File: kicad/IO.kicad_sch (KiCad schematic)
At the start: 40 parts, among them J3 Conn_02x10_Odd_Even, J4 Conn_02x10_Odd_Even, J5 Conn_02x10_Odd_Even, U12 ULN2803A

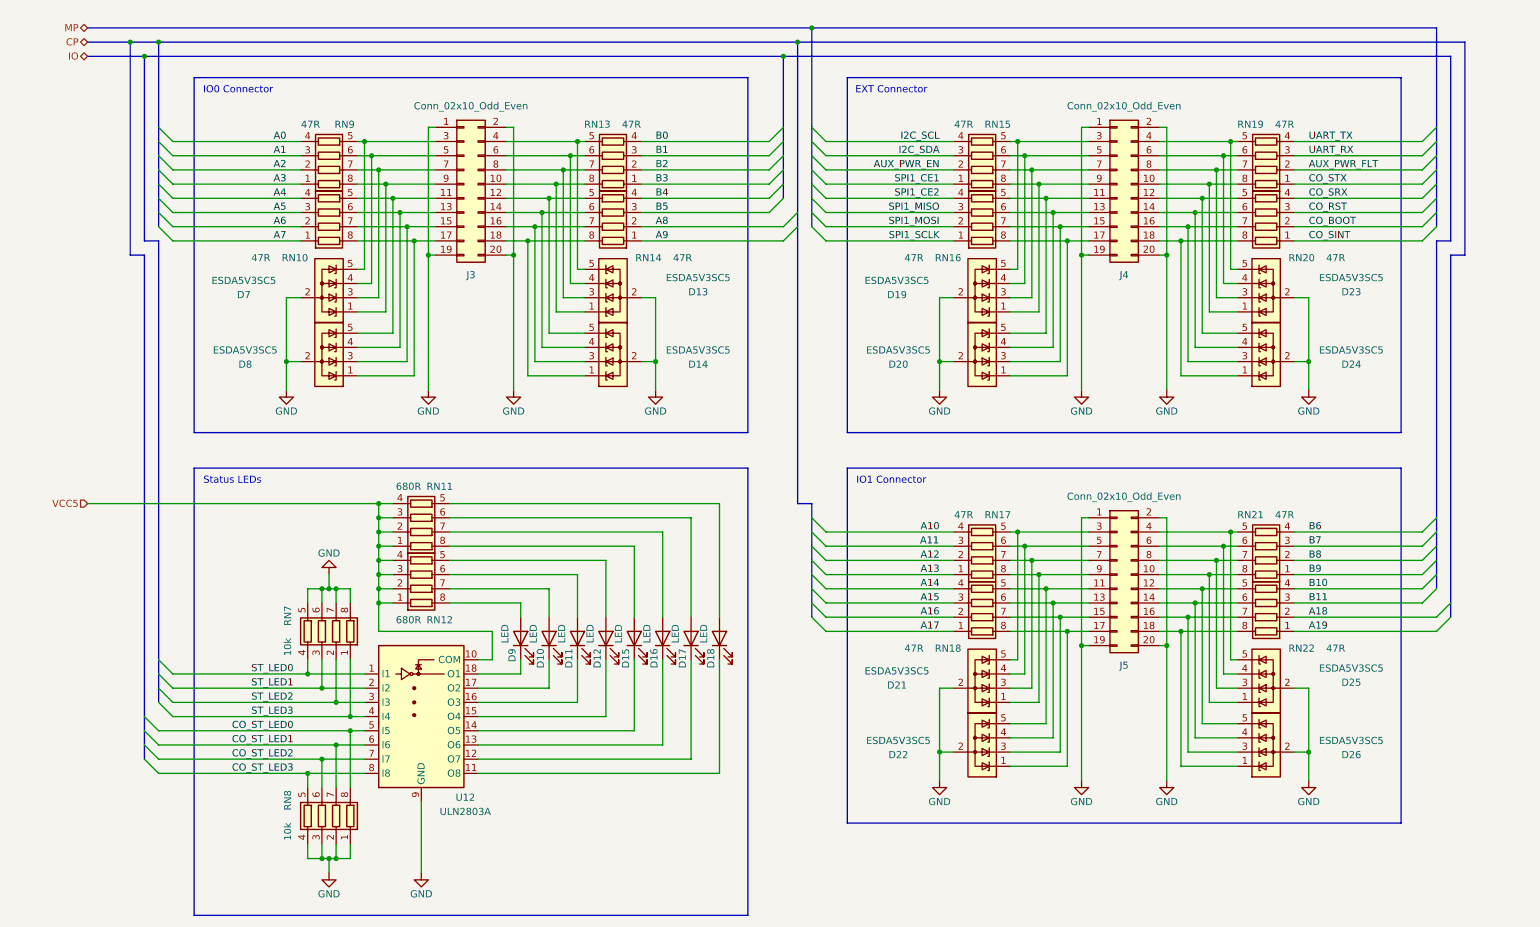
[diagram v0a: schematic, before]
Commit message: Add main bus to root schematic, use bus labels for exporting IO and CPIO busses
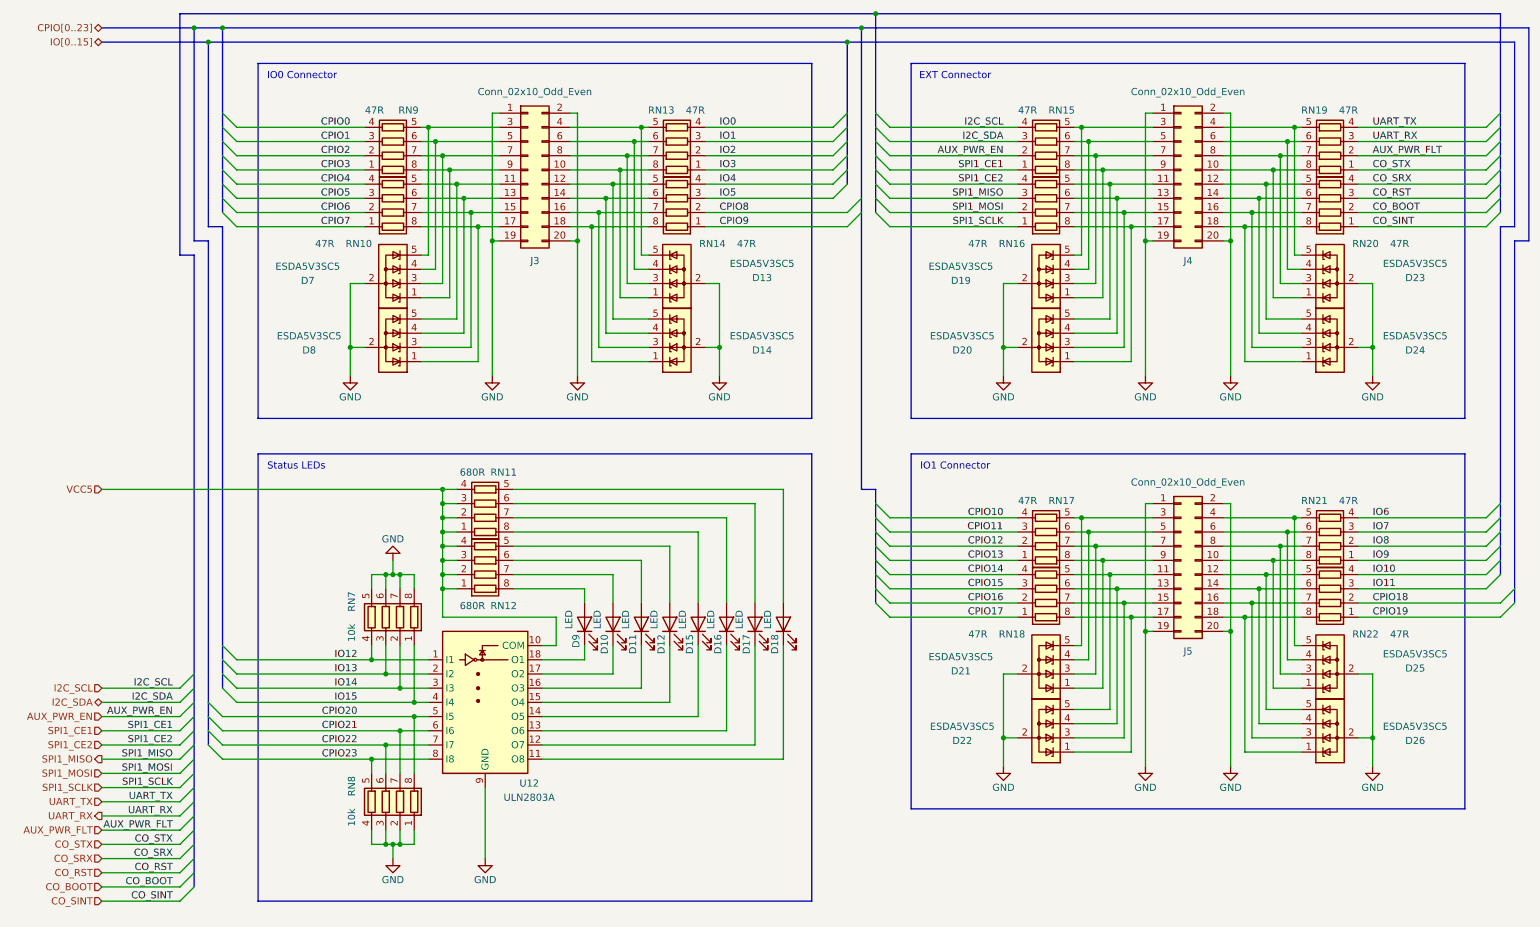
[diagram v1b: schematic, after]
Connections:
- net A0 renamed CPIO0
- net A1 renamed CPIO1
- net A10 renamed CPIO10
- net A11 renamed CPIO11
- net A12 renamed CPIO12
- net A13 renamed CPIO13
- net A14 renamed CPIO14
- net A15 renamed CPIO15
- net A16 renamed CPIO16
- net A17 renamed CPIO17
- net A18 renamed CPIO18
- net A19 renamed CPIO19
- net A2 renamed CPIO2
- net A3 renamed CPIO3
- net A4 renamed CPIO4
- net A5 renamed CPIO5
- net A6 renamed CPIO6
- net A7 renamed CPIO7
- net A8 renamed CPIO8
- net A9 renamed CPIO9
- net B0 renamed IO0
- net B1 renamed IO1
- net B10 renamed IO10
- net B11 renamed IO11
- net B2 renamed IO2
- net B3 renamed IO3
- net B4 renamed IO4
- net B5 renamed IO5
- net B6 renamed IO6
- net B7 renamed IO7
- net B8 renamed IO8
- net B9 renamed IO9
- net CO_ST_LED0 renamed CPIO20
- net CO_ST_LED1 renamed CPIO21
- net CO_ST_LED2 renamed CPIO22
- net CO_ST_LED3 renamed CPIO23
- net ST_LED0 renamed IO12
- net ST_LED1 renamed IO13
- net ST_LED2 renamed IO14
- net ST_LED3 renamed IO15
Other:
- moved on the sheet: D10, D11, D12, D13, D14, D15, D16, D17, D18, D19, D20, D21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

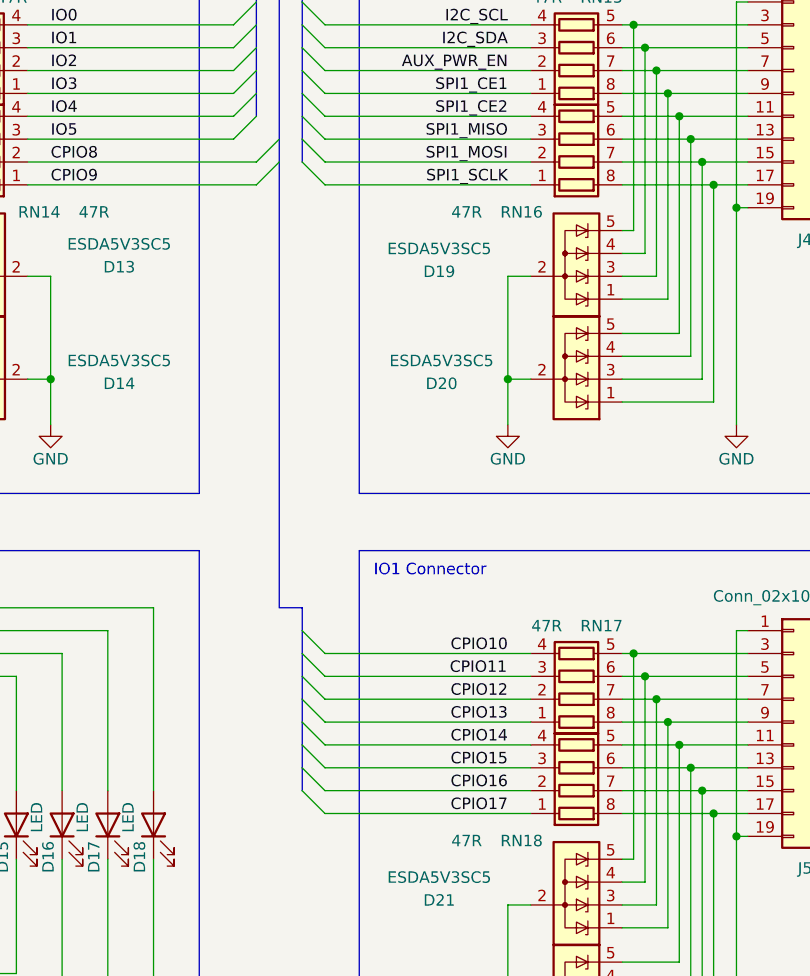
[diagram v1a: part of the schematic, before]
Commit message: Add EtherKraken V1 Rev. C schematics as PDF to docs
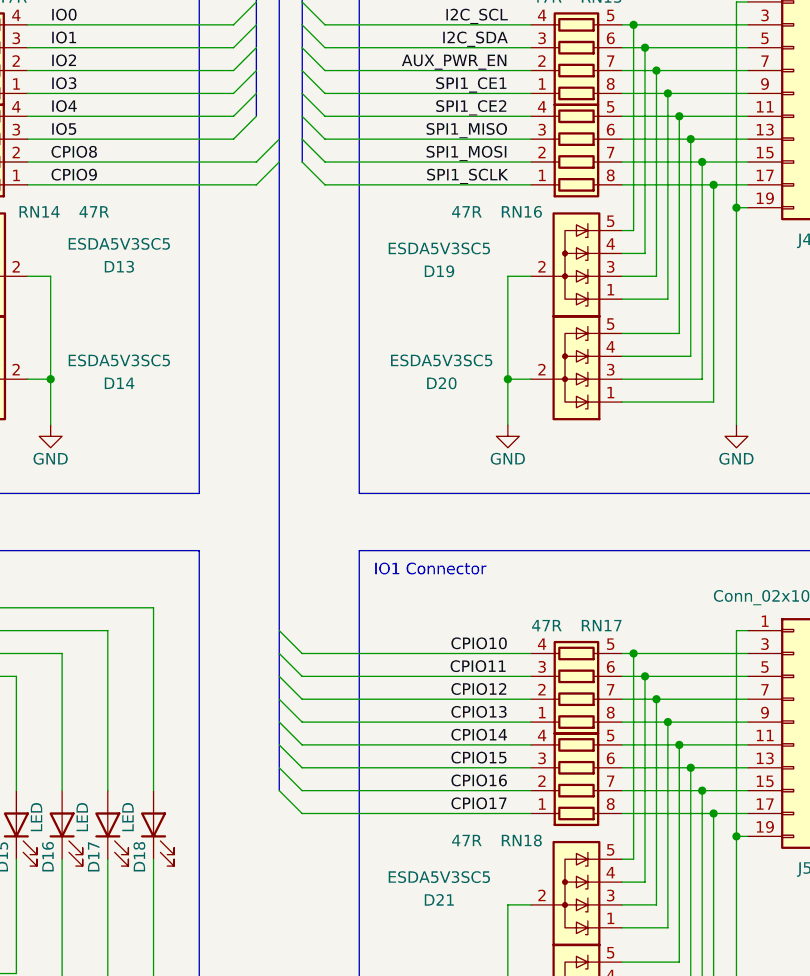
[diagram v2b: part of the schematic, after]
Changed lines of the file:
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@@
 	)
 	(bus_entry
-		(at 166.37 123.19)
+		(at 163.83 123.19)
 		(size 2.54 2.54)
 		(stroke
@@
 	)
 	(bus_entry
-		(at 166.37 105.41)
+		(at 163.83 105.41)
 		(size 2.54 2.54)
 		(stroke
@@
 	)
 	(bus_entry
-		(at 166.37 113.03)
+		(at 163.83 113.03)
 		(size 2.54 2.54)
 		(stroke
@@
 	)
 	(bus_entry
-		(at 166.37 120.65)
+		(at 163.83 120.65)
 		(size 2.54 2.54)
 		(stroke
@@
 	)
 	(bus_entry
-		(at 166.37 118.11)
+		(at 163.83 118.11)
 		(size 2.54 2.54)
 		(stroke
@@
 	)
 	(bus_entry
-		(at 166.37 110.49)
+		(at 163.83 110.49)
 		(size 2.54 2.54)
 		(stroke
@@
 	)
 	(bus_entry
-		(at 166.37 115.57)
+		(at 163.83 115.57)
 		(size 2.54 2.54)
 		(stroke
@@
 	)
 	(bus_entry
-		(at 166.37 107.95)
+		(at 163.83 107.95)
 		(size 2.54 2.54)
 		(stroke
@@
 	(wire
 		(pts
-			(xy 168.91 110.49) (xy 191.77 110.49)
+			(xy 166.37 110.49) (xy 191.77 110.49)
 		)
 		(stroke
@@
 	(wire
 		(pts
-			(xy 168.91 123.19) (xy 191.77 123.19)
+			(xy 166.37 123.19) (xy 191.77 123.19)
 		)
 		(stroke
@@
 		)
 	)
-	(bus
-		(pts
-			(xy 163.83 53.34) (xy 163.83 102.87)
-		)
-		(stroke
-			(width 0)
-			(type default)
-		)
-	)
 	(wire
 		(pts
@@
 	(wire
 		(pts
-			(xy 168.91 107.95) (xy 191.77 107.95)
+			(xy 166.37 107.95) (xy 191.77 107.95)
 		)
 		(stroke
@@
 	(wire
 		(pts
-			(xy 168.91 115.57) (xy 191.77 115.57)
+			(xy 166.37 115.57) (xy 191.77 115.57)
 		)
 		(stroke
@@
 	(wire
 		(pts
-			(xy 168.91 113.03) (xy 191.77 113.03)
+			(xy 166.37 113.03) (xy 191.77 113.03)
 		)
 		(stroke
@@
 	(wire
 		(pts
-			(xy 168.91 120.65) (xy 191.77 120.65)
+			(xy 166.37 120.65) (xy 191.77 120.65)
 		)
 		(stroke
@@
 		)
 	)
-	(bus
-		(pts
-			(xy 166.37 102.87) (xy 163.83 102.87)
-		)
-		(stroke
-			(width 0)
-			(type default)
-		)
-	)
 	(wire
 		(pts
@@
 	(wire
 		(pts
-			(xy 168.91 118.11) (xy 191.77 118.11)
+			(xy 166.37 118.11) (xy 191.77 118.11)
 		)
 		(stroke
@@
 	(wire
 		(pts
-			(xy 168.91 125.73) (xy 191.77 125.73)
+			(xy 166.37 125.73) (xy 191.77 125.73)
 		)
 		(stroke
@@
 	(bus
 		(pts
-			(xy 166.37 102.87) (xy 166.37 123.19)
+			(xy 163.83 53.34) (xy 163.83 123.19)
 		)
 		(stroke
